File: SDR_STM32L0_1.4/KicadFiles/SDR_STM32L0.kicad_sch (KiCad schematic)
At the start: 25 parts, among them SW1 SW_SPDT, U3 STM32L083VBTx, U4 AMS1117-3.3, Y1 32 MHz

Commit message: u
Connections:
- net USART2_CTX renamed USART2_CTS
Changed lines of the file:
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@@
 		)
 	)
-	(global_label "USART2_CTX"
+	(global_label "USART2_CTS"
 		(shape input)
 		(at 93.98 35.56 0)

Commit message: begin routing
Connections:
- net USART1_CTS: no longer names the net of U3.70 (PA11)
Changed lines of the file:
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@@
-	(wire
-		(pts
-			(xy 91.44 63.5) (xy 93.98 63.5)
-		)
-		(stroke
-			(width 0)
-			(type default)
-		)
-	)
 	(wire
 		(pts
@@
 				(hide yes)
 			)
-		)
-	)
-	(global_label "USART1_CTS"
-		(shape input)
-		(at 93.98 63.5 0)
-		(fields_autoplaced yes)
-		(effects
-			(font
-				(size 1.27 1.27)
-			)
-			(justify left)
-		)
-		(property "Intersheetrefs" "${INTERSHEET_REFS}"
-			(at 108.4556 63.5 0)
-			(effects
-				(font
-					(size 1.27 1.27)
-				)
-				(justify left)
-				(hide yes)
-			)

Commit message: Finished PCB Routing
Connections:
- net BP_INT: now also U3.46 (PE15); no longer U3.88 (PD7)
- net GPIO1_ADC: now also U3.54 (PB15); no longer U3.60 (PD13)
- net GPIO1_INPUT: now also U3.52 (PB13); no longer U3.62 (PD15)
- net GPIO1_OUTPUT: now also U3.53 (PB14); no longer U3.61 (PD14)
- net GPIO3_ADC: now also U3.83 (PD2); no longer U3.80 (PC12)
- net GPIO3_INPUT: now also U3.81 (PD0); no longer U3.78 (PC10)
- net GPIO3_OUTPUT: now also U3.82 (PD1); no longer U3.79 (PC11)
- net GPIO4_ADC: now also U3.17 (PC2); no longer U3.66 (PC9)
- net GPIO4_INPUT: now also U3.11 (PH10); no longer U3.64 (PC7)
- net GPIO4_OUTPUT: now also U3.18 (PC3); no longer U3.65 (PC8)
- net GPS_TIM: now also U3.71 (PA12); no longer U3.87 (PD6)
- net LPTIM1_OUT: now also U3.37 (PB2); no longer U3.16 (PC1)
- net LPUART1_RX: now also U3.34 (PC5); no longer U3.26 (PA3)
- net LPUART1_TX: now also U3.16 (PC1); no longer U3.25 (PA2)
- net USART2_RX: now also U3.26 (PA3); no longer U3.77 (PA15)
- net USART2_TX: now also U3.25 (PA2); no longer U3.86 (PD5)
- net SPI1_NSS: now reaches U3.41 (PE10)

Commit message: 1.5
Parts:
- removed C11: 10n, Capacitor_SMD:C_0402_1005Metric, symbol Device:C
- removed FB1: 120R, Inductor_SMD:L_0603_1608Metric, symbol Device:FerriteBead
- added BT3: 5V Battery, FlightComputer:MS621FE-FL11E, symbol Device:Battery_Cell
- added U8: 74AHC1G02, symbol 74xGxx:74AHC1G02
- C1, C2: value 70pF -> 25pF
- C13: value 1u -> 0.1u
- C6: value 22u -> 10u
- Y1: value 32 MHz -> 25 MHz
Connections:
- net +3.3VA is gone; now on net +3.3V: C13.1, U3.22 (VDDA)
- net +3.3V: now also C12.1
- net BP_INT: now also U3.41 (PE10); no longer U3.46 (PE15)
- net GND: now also BT3.2 (-), U8.3 (GND)
- net LPUART1_TX: now also U3.33 (PC4); no longer U3.16 (PC1)
- net SPI1_MOSI: now also U3.46 (PE15); no longer U3.32 (PA7)
- net SPI1_NSS: now also U3.43 (PE12); no longer U3.41 (PE10)
- net SPI1_SCK: now also U3.44 (PE13); no longer U3.30 (PA5)
- net VBUS: now also U8.2; no longer BT2.1 (+), C6.1, U4.3 (VI)
- net USART2_CTS renamed ROUTPUT
- net USART2_RX renamed BOUTPUT
- net USART2_TX renamed GOUTPUT
- new net: BT3.1 (+), U8.5 (VCC)
- new net: C6.1, U4.3 (VI), U8.4
- new net: BT2.1 (+), U8.1
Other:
- note added: "STM32 CHIP L083VBT"
- note removed: "STM32 CHIP L010RBTx"
- moved on the sheet: BT2, C1, C10, C2, C6, D1, H1, H2, H3, H4, R1, U4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

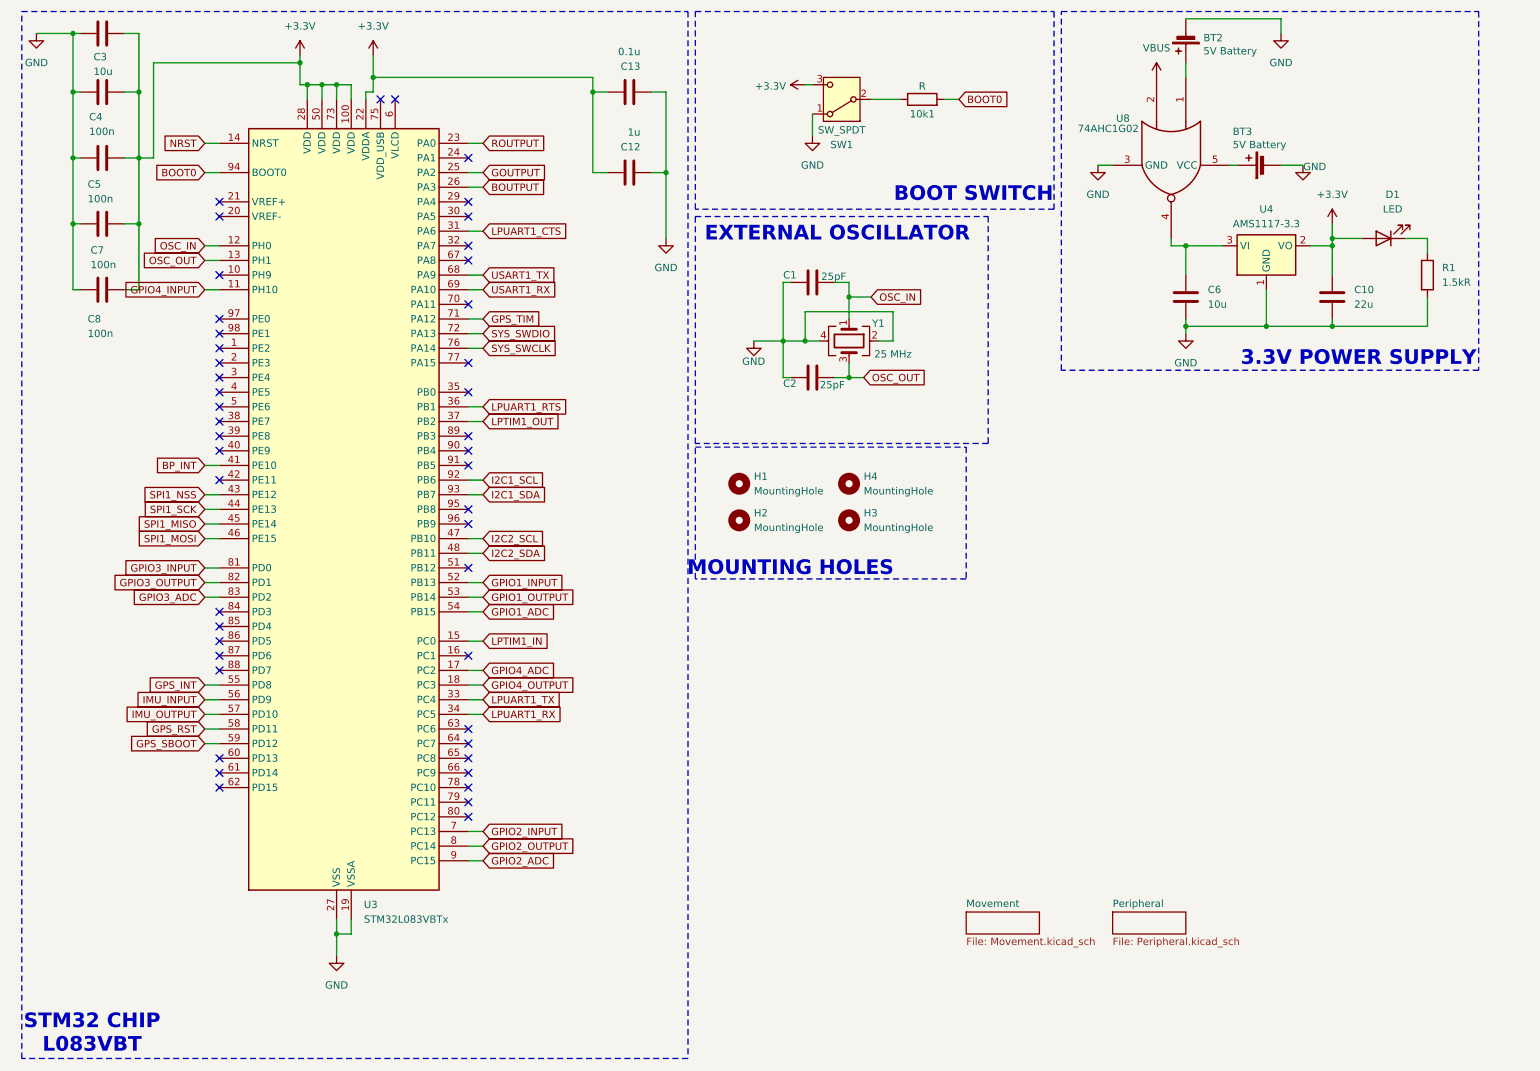
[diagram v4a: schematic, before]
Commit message: Upgrade
Changed a few peripherals (less ports, +/- on ports, switched jumpers, switched pinouts), and made new shematic
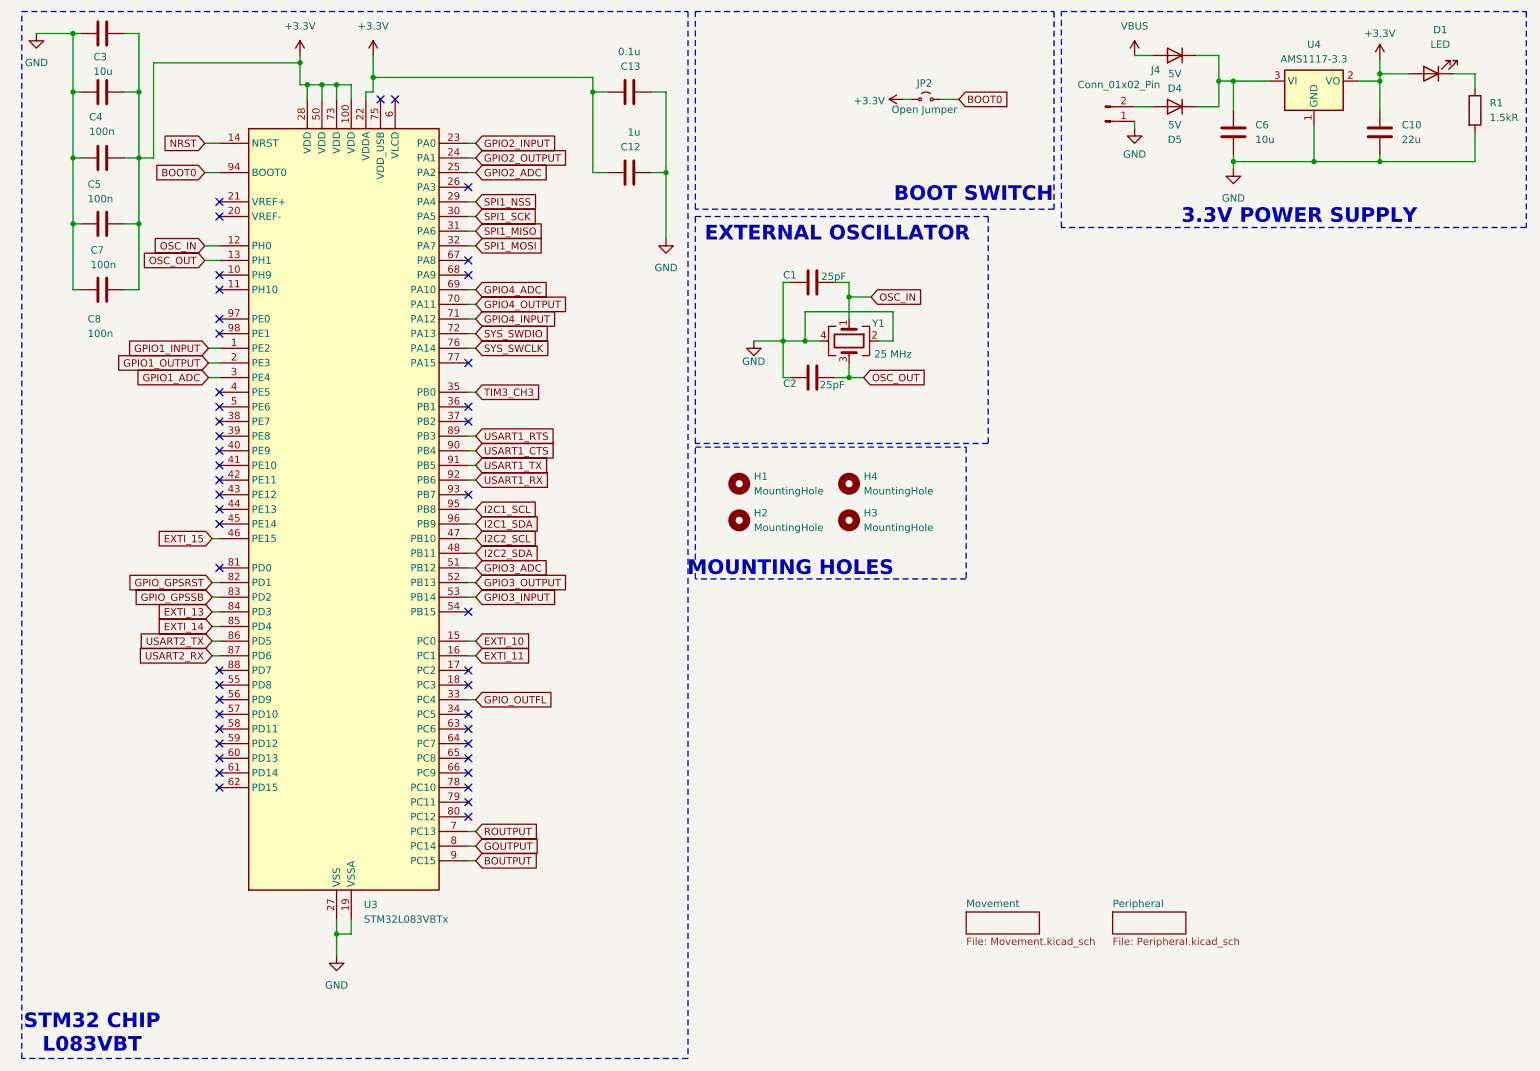
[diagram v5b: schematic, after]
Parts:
- removed 10k1: R, Resistor_SMD:R_0402_1005Metric, symbol Device:R
- removed BT2, BT3: 5V Battery, FlightComputer:MS621FE-FL11E, symbol Device:Battery_Cell
- removed SW1: SW_SPDT, Button_Switch_SMD:SW_SPST_B3U-1100P-B, symbol Switch:SW_SPDT
- removed U8: 74AHC1G02, symbol 74xGxx:74AHC1G02
- added D4, D5: 5V, Diode_SMD:D_SOD-123F, symbol Device:D
- added J4: Conn_01x02_Pin, 647676_2:CONN2_647676-2_TEC, symbol Connector:Conn_01x02_Pin
- added JP2: Open Jumper, Resistor_SMD:R_0603_1608Metric, symbol Jumper:Jumper_2_Small_Open
- C1, C2, C4, C5, C7, C8: footprint Capacitor_SMD:C_0402_1005Metric -> Capacitor_SMD:C_0603_1608Metric
- R1: footprint Resistor_SMD:R_0402_1005Metric -> Resistor_SMD:R_0603_1608Metric
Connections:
- net GPS_TIM is gone; now on net GPIO4_INPUT: U3.71 (PA12)
- net LPUART1_CTS is gone; now on net SPI1_MISO: U3.31 (PA6)
- net +3.3V: now also JP2.1 (A)
- net BOOT0: now also JP2.2 (B)
- net BOUTPUT: now also U3.9 (PC15); no longer U3.26 (PA3)
- net GND: now also J4.1 (Pin_1)
- net GOUTPUT: now also U3.8 (PC14); no longer U3.25 (PA2)
- net GPIO1_ADC: now also U3.3 (PE4); no longer U3.54 (PB15)
- net GPIO1_INPUT: now also U3.1 (PE2); no longer U3.52 (PB13)
- net GPIO1_OUTPUT: now also U3.2 (PE3); no longer U3.53 (PB14)
- net GPIO2_ADC: now also U3.25 (PA2); no longer U3.9 (PC15)
- net GPIO2_INPUT: now also U3.23 (PA0); no longer U3.7 (PC13)
- net GPIO2_OUTPUT: now also U3.24 (PA1); no longer U3.8 (PC14)
- net GPIO3_ADC: now also U3.51 (PB12); no longer U3.83 (PD2)
- net GPIO3_INPUT: now also U3.53 (PB14); no longer U3.81 (PD0)
- net GPIO3_OUTPUT: now also U3.52 (PB13); no longer U3.82 (PD1)
- net GPIO4_ADC: now also U3.69 (PA10); no longer U3.17 (PC2)
- net GPIO4_INPUT: no longer U3.11 (PH10)
- net GPIO4_OUTPUT: now also U3.70 (PA11); no longer U3.18 (PC3)
- net I2C1_SCL: now also U3.95 (PB8); no longer U3.92 (PB6)
- net I2C1_SDA: now also U3.96 (PB9); no longer U3.93 (PB7)
- net ROUTPUT: now also U3.7 (PC13); no longer U3.23 (PA0)
- net SPI1_MISO: no longer U3.45 (PE14)
- net SPI1_MOSI: now also U3.32 (PA7); no longer U3.46 (PE15)
- net SPI1_NSS: now also U3.29 (PA4); no longer U3.43 (PE12)
- net SPI1_SCK: now also U3.30 (PA5); no longer U3.44 (PE13)
- net USART1_RX: now also U3.92 (PB6); no longer U3.69 (PA10)
- net USART1_TX: now also U3.91 (PB5); no longer U3.68 (PA9)
- net VBUS: now also D4.2 (A)
- net EXTI_11: now reaches U3.16 (PC1)
- net TIM3_CH3: now reaches U3.35 (PB0)
- net EXTI_13: now reaches U3.84 (PD3)
- net EXTI_14: now reaches U3.85 (PD4)
- net USART2_TX: now reaches U3.86 (PD5)
- net USART2_RX: now reaches U3.87 (PD6)
- net USART1_RTS: now reaches U3.89 (PB3)
- net USART1_CTS: now reaches U3.90 (PB4)
- net at C6.1, U4.3 (VI): now also D4.1 (K), D5.1 (K)
- net BP_INT: no longer names the net of U3.41 (PE10)
- net GPS_INT: no longer names the net of U3.55 (PD8)
- net GPS_RST: no longer names the net of U3.58 (PD11)
- net GPS_SBOOT: no longer names the net of U3.59 (PD12)
- net IMU_INPUT: no longer names the net of U3.56 (PD9)
- net IMU_OUTPUT: no longer names the net of U3.57 (PD10)
- net LPTIM1_IN renamed EXTI_10
- net LPTIM1_OUT: no longer names the net of U3.37 (PB2)
- net LPUART1_RTS: no longer names the net of U3.36 (PB1)
- net LPUART1_RX: no longer names the net of U3.34 (PC5)
- net LPUART1_TX renamed GPIO_OUTFL
- new net: D5.2 (A), J4.2 (Pin_2)
- new net EXTI_15: U3.46 (PE15)
- new net GPIO_GPSRST: U3.82 (PD1)
- new net GPIO_GPSSB: U3.83 (PD2)
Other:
- moved on the sheet: C10, C6, D1, R1, U4
